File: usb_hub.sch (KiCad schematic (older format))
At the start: 13 parts, among them U1001 NX5P3090UKZ

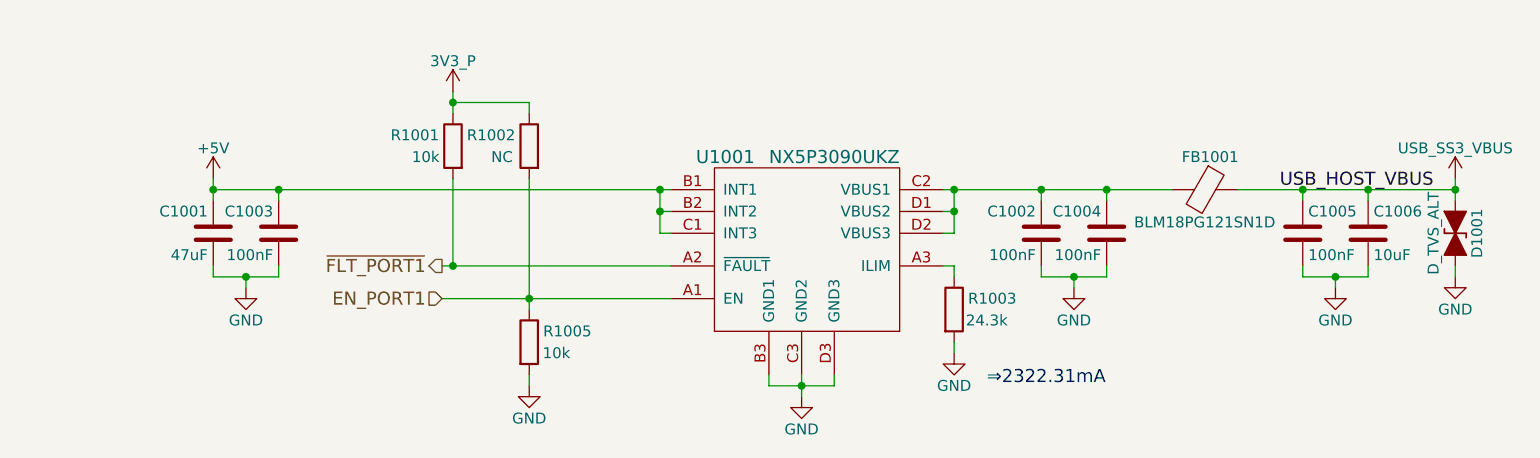
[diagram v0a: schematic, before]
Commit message: Add USB type C circuit with DRP PD capability, should sink near 2A @ 5-6.5V and source 550mA @ 5V
Removed the reverse current protection circuit from the last commit due to the requirement changing to only 18650 battery and USB-C being possible power sources

Next thing to add is the charging circuit when the USB-C is in sink mode/role
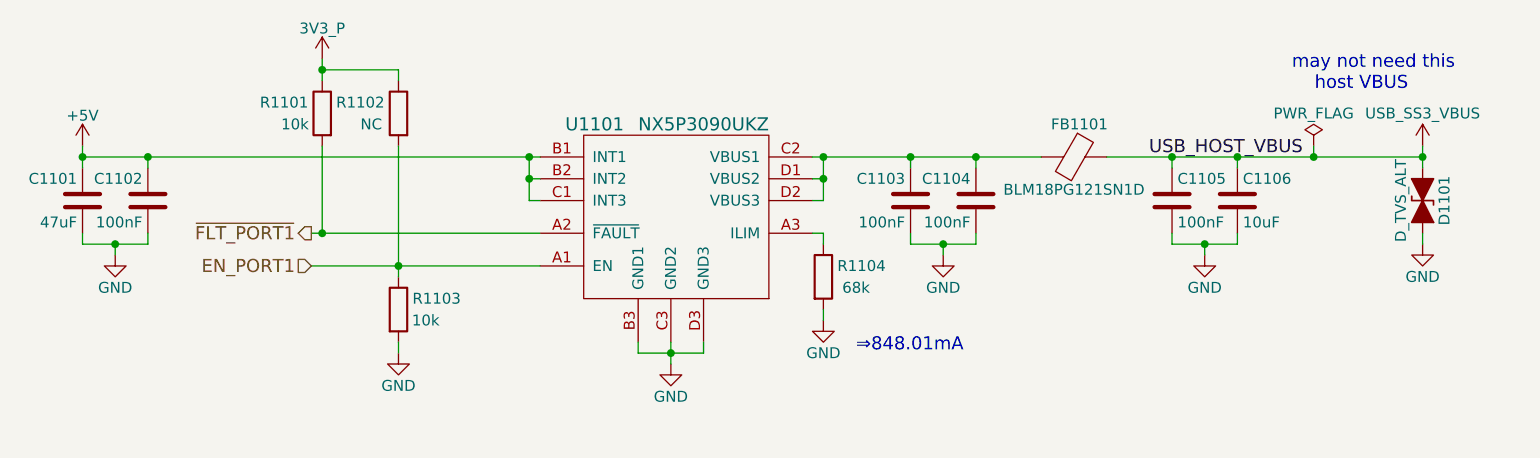
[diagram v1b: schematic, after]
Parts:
- removed C1001: 47uF, symbol C
- removed C1002, C1003, C1004, C1005: 100nF, symbol C
- removed C1006: 10uF, symbol C
- removed D1001: D_TVS_ALT, symbol D_TVS_ALT
- removed FB1001: BLM18PG121SN1D, symbol Ferrite_Bead
- removed R1001, R1005: 10k, symbol R
- removed R1002: NC, symbol R
- removed R1003: 24.3k, symbol R
- removed U1001: NX5P3090UKZ, symbol NX5P3090UKZ
- added C1101: 47uF, symbol C
- added C1102, C1103, C1104, C1105: 100nF, symbol C
- added C1106: 10uF, symbol C
- added D1101: D_TVS_ALT, symbol D_TVS_ALT
- added FB1101: BLM18PG121SN1D, symbol Ferrite_Bead
- added R1101, R1103: 10k, symbol R
- added R1102: NC, symbol R
- added R1104: 68k, symbol R
- added U1101: NX5P3090UKZ, symbol NX5P3090UKZ
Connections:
- net +5V: now also C1101.1, C1102.1, U1101.B1 (INT1), U1101.B2 (INT2), U1101.C1 (INT3)
- net 3V3_P: now also R1101.1, R1102.1
- net EN_PORT1: now also R1102.2, R1103.1, U1101.A1 (EN)
- net GND: now also C1101.2, C1102.2, C1103.2, C1104.2, C1105.2, C1106.2, D1101.2 (A2), R1103.2, R1104.2, U1101.B3 (GND1), U1101.C3 (GND2), U1101.D3 (GND3)
- net USB_SS3_VBUS: now also C1105.1, C1106.1, D1101.1 (A1), FB1101.1
- net ~FLT_PORT1: now also R1101.2, U1101.A2 (~FAULT)
- new net: R1104.1, U1101.A3 (ILIM)
- new net: C1103.1, C1104.1, FB1101.2, U1101.C2 (VBUS1), U1101.D1 (VBUS2), U1101.D2 (VBUS3)
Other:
- note added: "may not need this\n host VBUS"
- note added: "⇒848.01mA"
- note removed: "⇒2322.31mA"

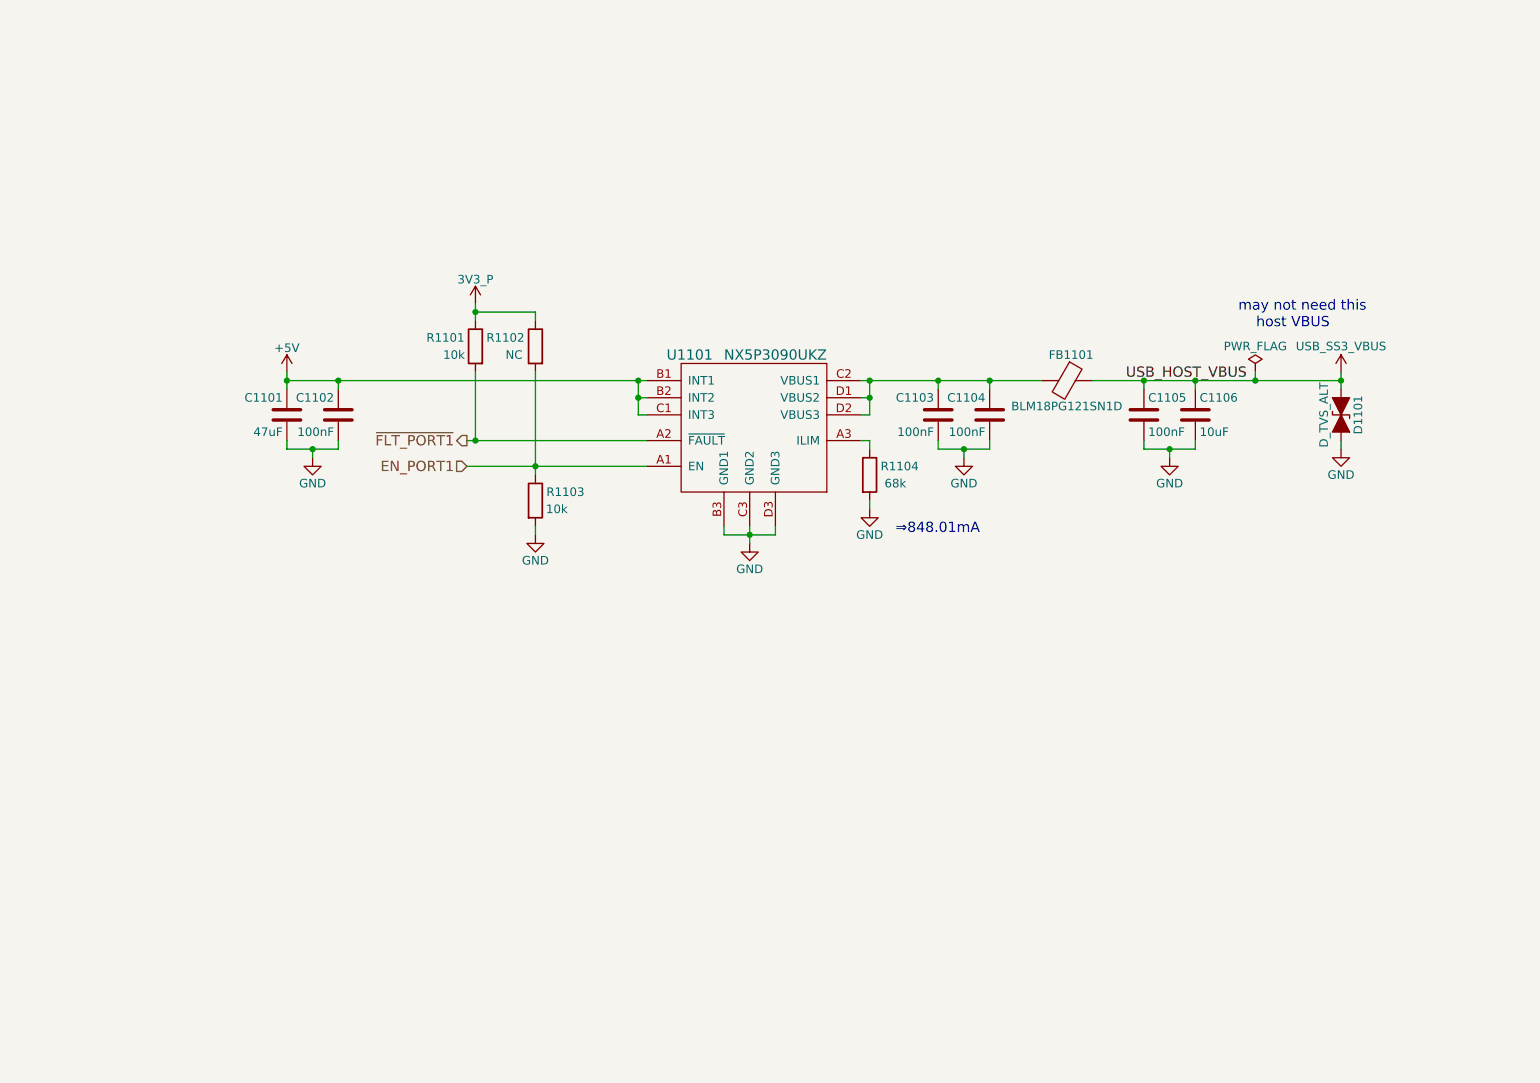
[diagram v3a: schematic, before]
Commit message: Begin USB 2.0 hub circuit for M.2 modules, remove supervisory/voltage monitor/watchdog circuit since the EmCraft SoM implements it
USB 2.0 hub circuit still needs to be completed.
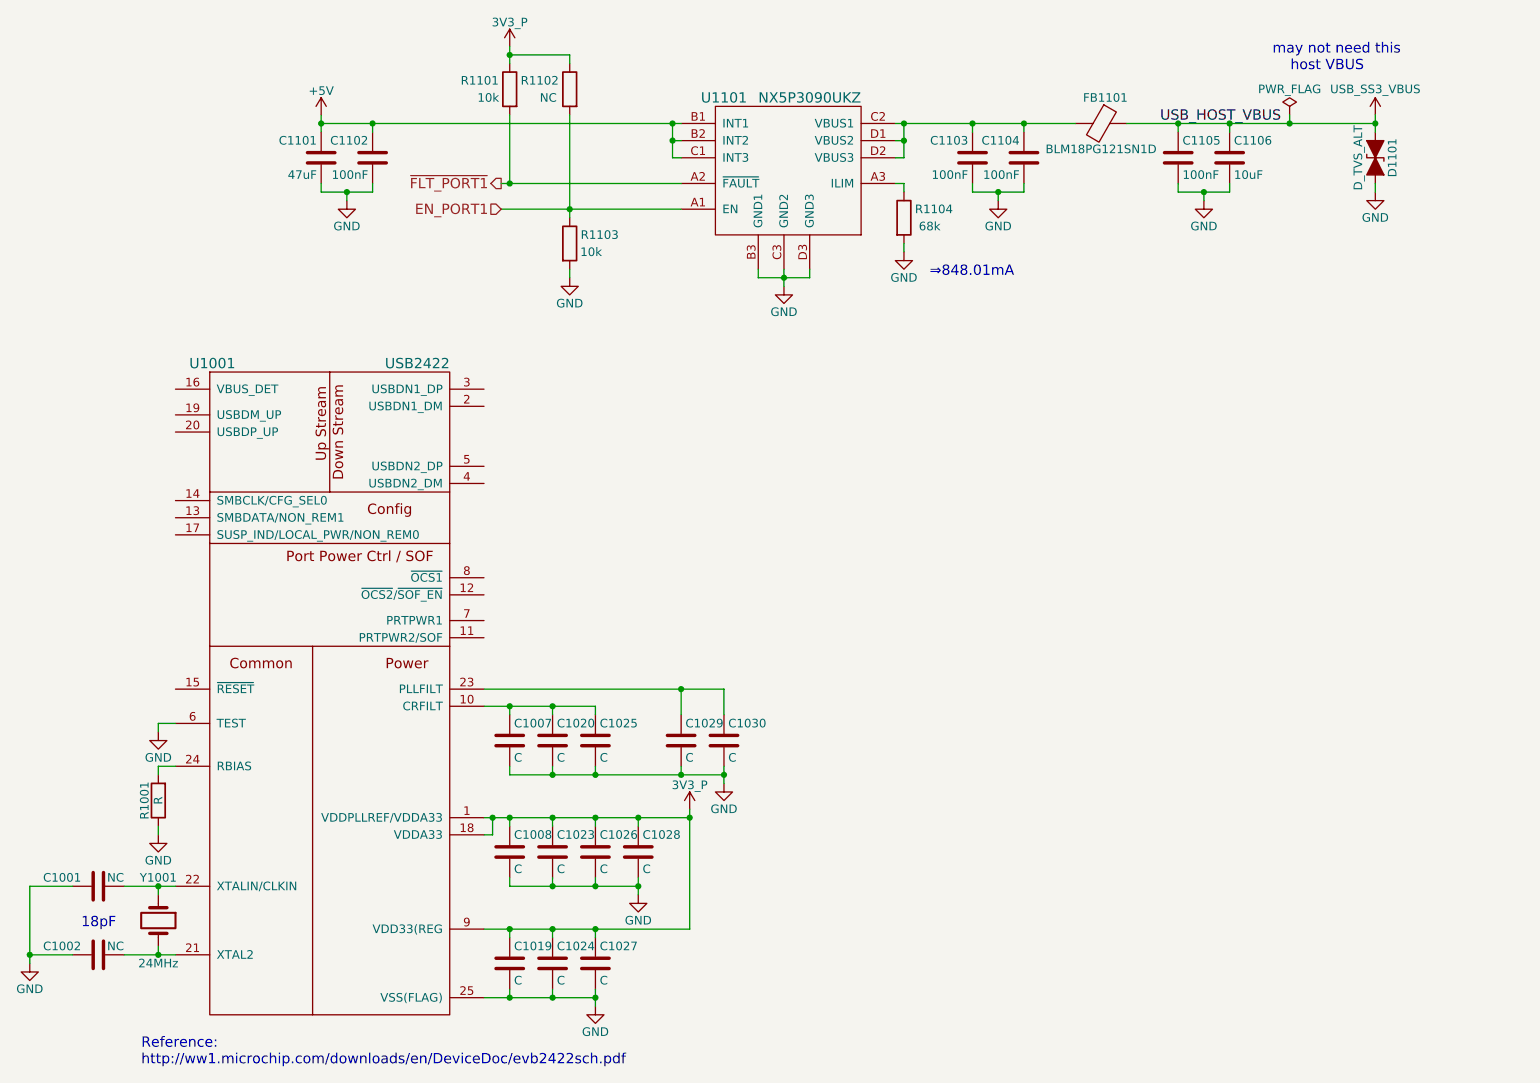
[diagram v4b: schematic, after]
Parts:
- added C1001, C1002: NC, symbol C
- added C1007, C1008, C1019, C1020, C1023, C1024, C1025, C1026, C1027, C1028, C1029, C1030: C, symbol C
- added R1001: R, symbol R
- added U1001: USB2422, symbol USB2422
- added Y1001: 24MHz, symbol Crystal
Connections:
- net 3V3_P: now also C1008.1, C1019.1, C1023.1, C1024.1, C1026.1, C1027.1, C1028.1, U1001.1 (VDDPLLREF/VDDA33), U1001.18 (VDDA33), U1001.9 (VDD33(REG)
- net GND: now also C1001.1, C1002.1, C1007.2, C1008.2, C1019.2, C1020.2, C1023.2, C1024.2, C1025.2, C1026.2, C1027.2, C1028.2, C1029.2, C1030.2, R1001.1, U1001.25 (VSS(FLAG)), U1001.6 (TEST)
- new net: C1007.1, C1020.1, C1025.1, U1001.10 (CRFILT)
- new net: C1002.2, U1001.21 (XTAL2), Y1001.2
- new net: C1001.2, U1001.22 (XTALIN/CLKIN), Y1001.1
- new net: C1029.1, C1030.1, U1001.23 (PLLFILT)
- new net: R1001.2, U1001.24 (RBIAS)
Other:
- note added: "18pF"
- note added: "Reference:\nhttp://ww1.microchip.com/downloads/en/DeviceDoc/evb2422sch.pdf"
- moved on the sheet: C1101, C1102, C1103, C1104, C1105, C1106, D1101, FB1101, R1101, R1102, R1103, R1104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

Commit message: Complete more of the USB hub circuit, connect one of the downstream ports to the WWAN M.2 module, remove the unused VBUS rail, add notes regarding the USB-C port having its corresponding ID pin pulled low
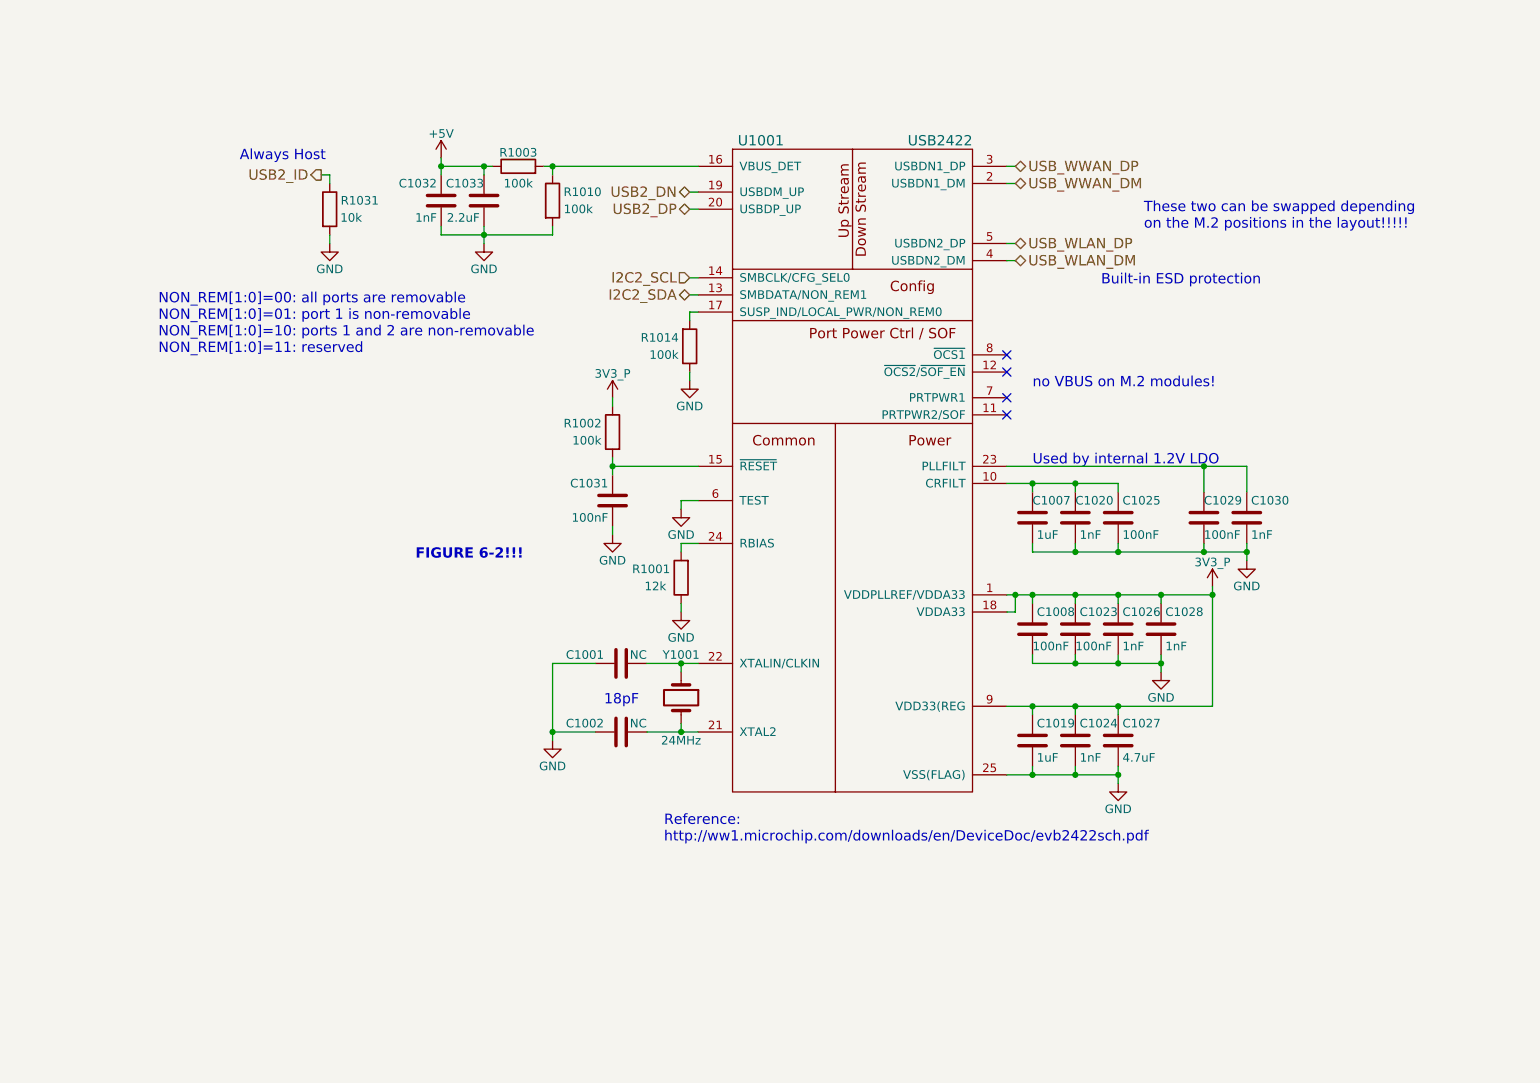
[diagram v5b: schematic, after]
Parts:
- removed C1101: 47uF, symbol C
- removed C1102, C1103, C1104, C1105: 100nF, symbol C
- removed C1106: 10uF, symbol C
- removed D1101: D_TVS_ALT, symbol D_TVS_ALT
- removed FB1101: BLM18PG121SN1D, symbol Ferrite_Bead
- removed R1101, R1103: 10k, symbol R
- removed R1102: NC, symbol R
- removed R1104: 68k, symbol R
- removed U1101: NX5P3090UKZ, symbol NX5P3090UKZ
- added C1031: 100nF, symbol C
- added C1032: 1nF, symbol C
- added C1033: 2.2uF, symbol C
- added R1002, R1003, R1010, R1014: 100k, symbol R
- added R1031: 10k, symbol R
- C1007, C1019: value C -> 1uF
- C1008, C1023, C1025, C1029: value C -> 100nF
- C1020, C1024, C1026, C1028, C1030: value C -> 1nF
- C1027: value C -> 4.7uF
- R1001: value R -> 12k
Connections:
- net +5V: now also C1032.1, C1033.1, R1003.1
- net 3V3_P: now also R1002.1
- net GND: now also C1031.2, C1032.2, C1033.2, R1010.2, R1014.1, R1031.2
- net I2C2_SDA: now reaches U1001.13 (SMBDATA/NON_REM1)
- net I2C2_SCL: now reaches U1001.14 (SMBCLK/CFG_SEL0)
- net at U1001.15 (~RESET): now also C1031.1, R1002.2
- net at U1001.16 (VBUS_DET): now also R1003.2, R1010.1
- net at U1001.17 (SUSP_IND/LOCAL_PWR/NON_REM0): now also R1014.2
- net USB2_DN: now reaches U1001.19 (USBDM_UP)
- net USB_WWAN_DM: now reaches U1001.2 (USBDN1_DM)
- net USB2_DP: now reaches U1001.20 (USBDP_UP)
- net USB_WWAN_DP: now reaches U1001.3 (USBDN1_DP)
- net USB_WLAN_DM: now reaches U1001.4 (USBDN2_DM)
- net USB_WLAN_DP: now reaches U1001.5 (USBDN2_DP)
- new net USB2_ID: R1031.1
- no-connect marks 0 -> 4
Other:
- note added: "Always Host"
- note added: "Built-in ESD protection"
- note added: "FIGURE 6-2!!!"
- note added: "NON_REM[1:0]=00: all ports are removable\nNON_REM[1:0]=01: port 1 is non-removable\nNON_REM[1:0]=10: ports 1 and 2 are non-removable\nNON_REM[1:0]=11: reserved"
- note added: "These two can be swapped depending\non the M.2 positions in the layout!!!!!"
- note added: "Used by internal 1.2V LDO"
- note added: "no VBUS on M.2 modules!"
- note removed: "may not need this\n host VBUS"
- note removed: "⇒848.01mA"
- moved on the sheet: C1001, C1002, C1007, C1008, C1019, C1020, C1023, C1024, C1025, C1026, C1027, C1028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
